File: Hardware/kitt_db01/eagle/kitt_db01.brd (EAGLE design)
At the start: 74.3 x 53.3 mm, 100 parts, among them U9.00 ADNS-3080, U9.01 MIC5205-3.3YM5TR, U9.02 SI1922EDH, X9.00 RESON

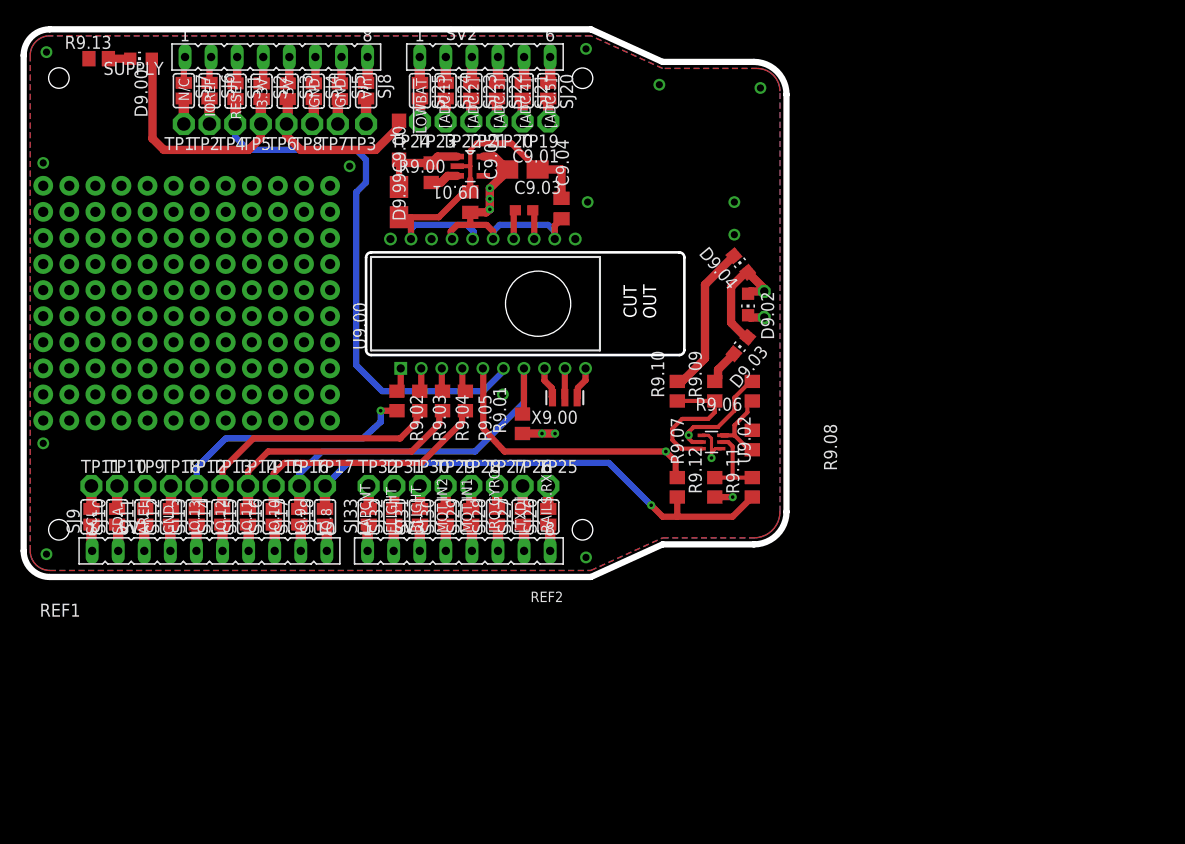
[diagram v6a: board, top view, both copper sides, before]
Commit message: updated bom; added pullups and a double I2C header
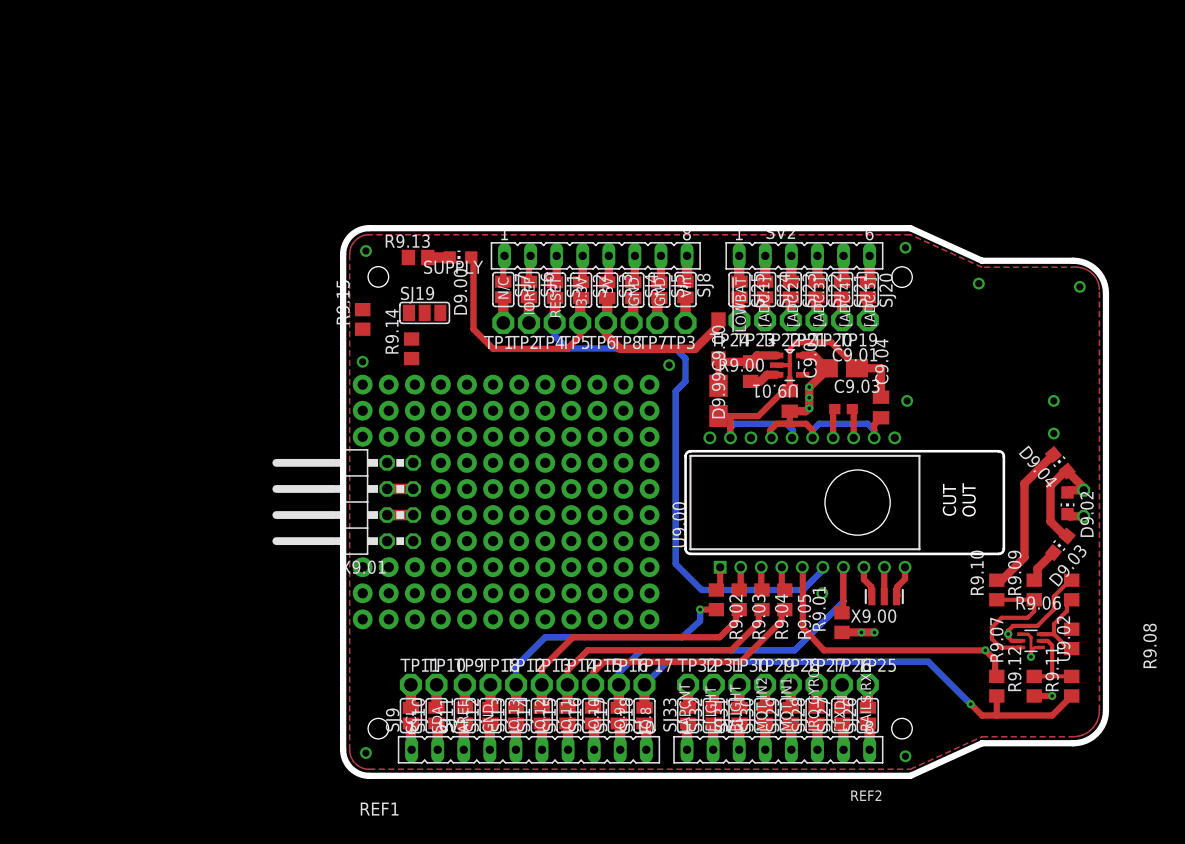
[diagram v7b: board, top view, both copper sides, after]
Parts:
- added R9.14, R9.15: 10kR, rcl:R0805
- added SJ19: (no value), jumper:SJ_2
- added X9.01: (no value), pinhead:2X04/90
- moved C9.00 36.7 mm to (61.3, 49.5)
- moved C9.01 36.7 mm to (73.3, 52.7)
- moved C9.03 36.7 mm to (73.5, 48.7)
- moved C9.04 36.7 mm to (77.2, 48.9)
- moved C9.05 36.7 mm to (68.3, 49.5)
- moved D9.00 36.7 mm to (36.2, 63.5)
- moved D9.99 36.7 mm to (61.3, 55.6)
- moved R9.00 36.7 mm to (64.5, 52.4)
- moved R9.01 36.7 mm to (73.3, 27.9)
- moved R9.03 36.7 mm to (63.3, 30.2)
- moved R9.04 36.7 mm to (65.6, 30.2)
- moved R9.09 36.7 mm to (92.1, 31.1)
- moved R9.12 36.7 mm to (92.1, 21.7)
- moved R9.13 36.7 mm to (32.1, 63.5)
- moved SJ1 36.7 mm to (45.4, 60.3)
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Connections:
- new net N$44: R9.14.2, R9.15.2, SJ19.2, X9.01.7, X9.01.8
- net +3V3: now also SJ19.1
- net +5V: now also SJ19.3
- net GND: now also X9.01.1, X9.01.2
- net SCL: now also R9.15.1, X9.01.3, X9.01.4
- net SDA: now also R9.14.1, X9.01.5, X9.01.6
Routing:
- net +5V: track 16.7 -> 25.2 mm
- net SCL: track 2.24 -> 7.38 mm
- net GND: track 47.4 -> 50.1 mm, vias 14 -> 13
- net SDA: track 2.24 -> 4.78 mm
- net N$44: track 0.00 -> 2.54 mm, vias 1 -> 0
- net +3V3: track 149.2 -> 148.7 mm
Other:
- outline, holes or cut-outs redrawn

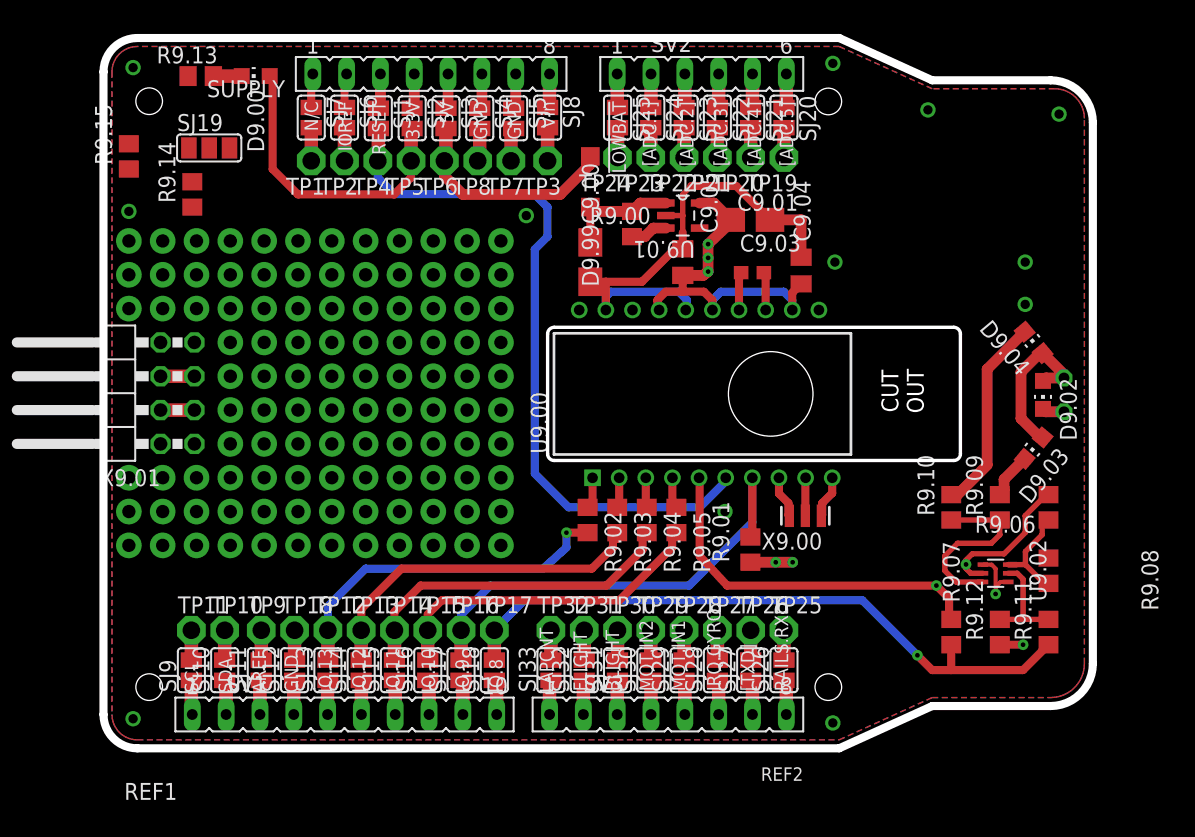
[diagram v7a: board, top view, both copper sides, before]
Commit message: snapshot of db01 board layout -> placement of top and bottom silkscreen acceptable -> todo: flip solderbridges on patching areas to bottom,    and also flip pin text to top
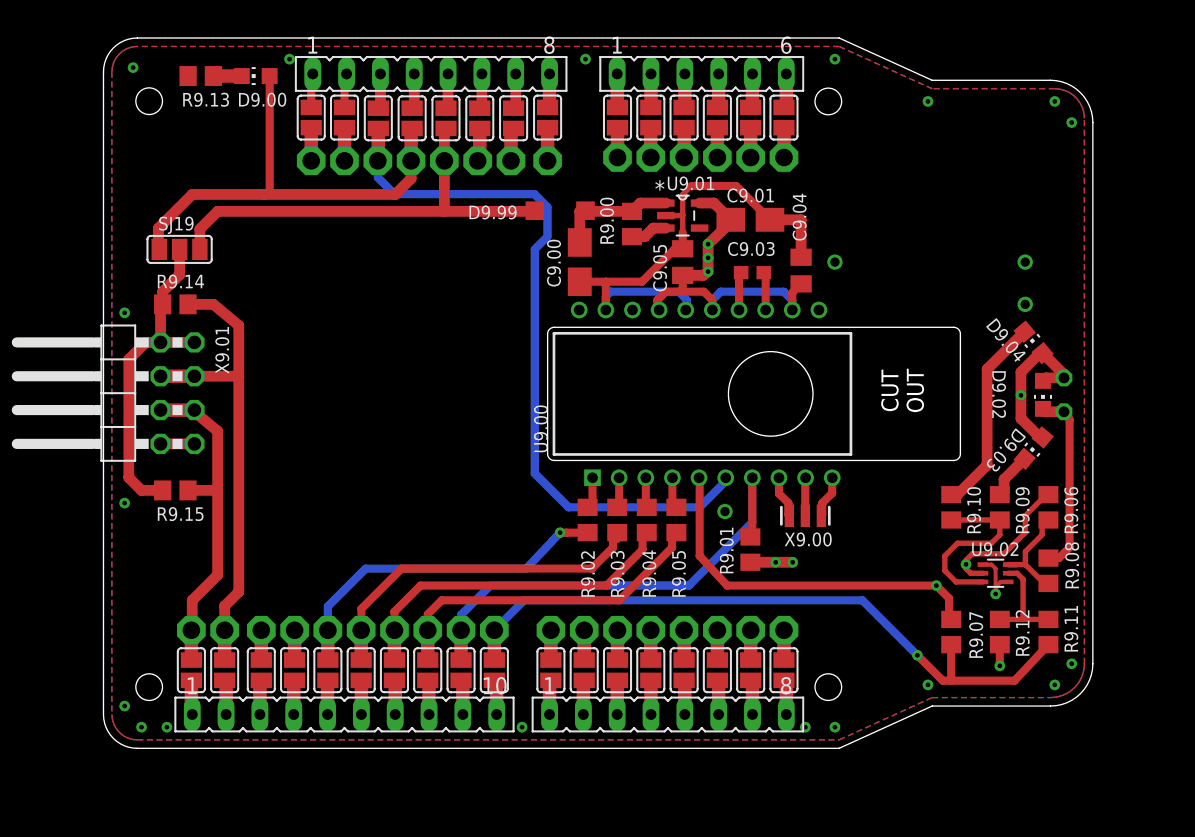
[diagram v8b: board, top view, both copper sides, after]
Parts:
- removed REF1: REF.KITT-DB01, kitt.refs:REF_KITT-DB01
- removed REF2: REF_GC-BBV2.0, kitt.con:REF_GHOSTCAR
- moved R9.15 25.3 mm to (30.2, 32.4), turned to 180 degrees
- moved R9.14 8.35 mm to (30.2, 46.4), turned to 180 degrees
- moved SJ19 7.94 mm to (30.5, 50.5)
- moved D9.99 3.14 mm to (59.1, 53.4), turned to 180 degrees
- moved C9.00 0.79 mm to (60.5, 49.5)
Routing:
- net SDA: track 4.78 -> 35.8 mm
- net N$44: track 2.54 -> 24.9 mm
- net SCL: track 7.38 -> 25.2 mm
- net N$8: track 1.75 -> 14.0 mm
- net +3V3: track 148.7 -> 160.8 mm, vias 5 -> 6
- net +5V: track 25.2 -> 33.6 mm
- net AUXLED: track 55.3 -> 57.5 mm
- net !LEDCTRL: track 49.7 -> 51.2 mm
- net GND: track 50.1 -> 50.7 mm, vias 13 -> 23
- net !CS: track 26.5 -> 25.9 mm
- removed copper zone on layer 2, net GND1
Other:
- board text added: "+3V3"
- board text added: "+5V0"
- board text added: "+VIN"
- board text added: "ADC0"
- board text added: "ADC1"
- board text added: "ADC2"
- board text added: "ADC3"
- board text added: "ADC4"
- board text added: "ADC5"
- board text added: "AREF"
- board text added: "GND"
- board text added: "IO00"
- board text added: "IO01"
- board text added: "IO02"
- board text added: "IO03"
- board text added: "IO04"
- board text added: "IO05"
- board text added: "IO06"
- board text added: "IO07"
- board text added: "IO08"
- board text added: "IO09"
- board text added: "IO10"
- board text added: "IO11"
- board text added: "IO12"
- board text added: "IO13"
- board text added: "IOR"
- board text added: "N/C"
- board text added: "RST"
- board text added: "SCL"
- board text added: "SDA"
